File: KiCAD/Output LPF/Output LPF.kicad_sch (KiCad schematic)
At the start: 55 parts, among them J1 Conn_Coaxial_Small, J2 8P8C_Shielded, J28 Filter In, K1 G6K-2P-Y-T1, K2 G6K-2P-Y-T1, K3 G6K-2P-Y-T1, K4 G6K-2P-Y-T1, Q1 2N7000, Q10 2N7000, Q5 2N7000, Q8 2N7000

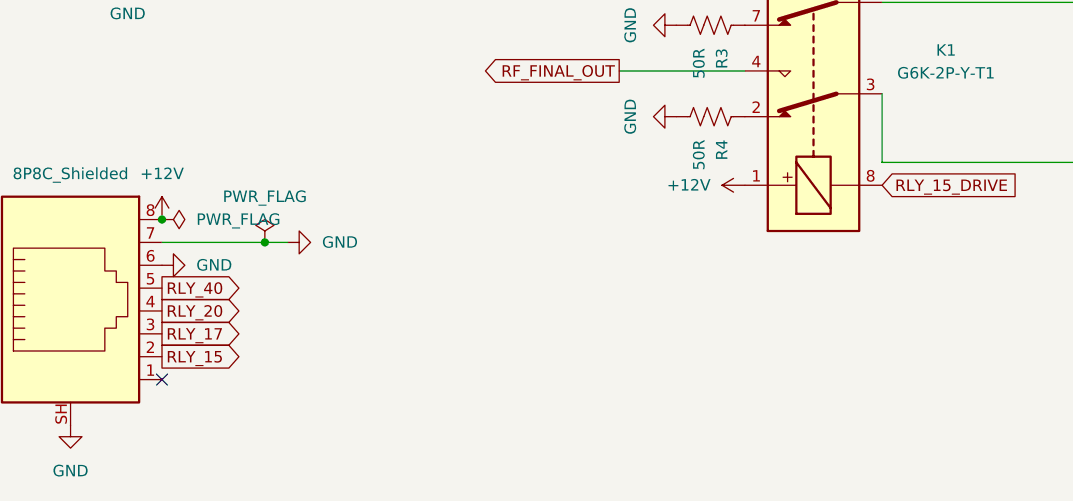
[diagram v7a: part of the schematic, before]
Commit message: revD: frontpanel + Output LPF text updates + protoshield in-progress
Output LPF: K relay Description text fix (pole 2 NC/COM/NO -> NO/COM/NC)
on K1/K2/K3 instances and the embedded lib symbol; CF7/CF8/CF12/CF16
Description "Unpolarized capacitor 2 in parallel to reach" stripped
back to "Unpolarized capacitor"; L6-L20 Descriptions updated T68-6 ->
T50-6 to match footprints.

xmitter.kicad_sym Relay_G6K Description text fix (pole 2 NC/COM/NO ->
NO/COM/NC) so future placements come out right.

Frontpanel: user updates (netlist regenerated).

Protoshield: in-progress schematic touches (new J7, #PWR017). Netlist
intentionally stale -- will regen after Metro-symbol SDA/SCL addition.

Co-Authored-By: Claude Opus 4.7 <noreply@anthropic.com>
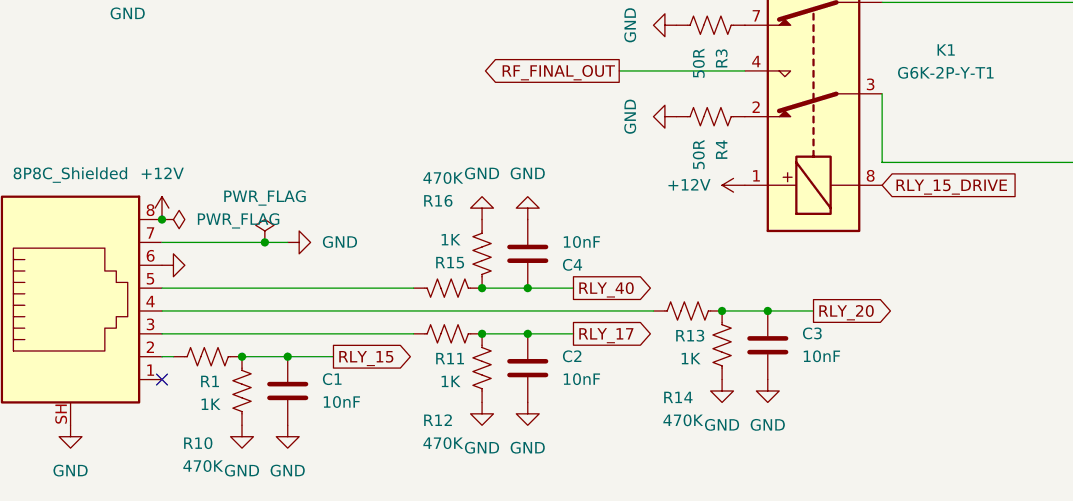
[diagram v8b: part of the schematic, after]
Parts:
- added C1, C2, C3, C4: 10nF, symbol Device:C
- added R1, R11, R13, R15: 1K, symbol Device:R_US
- added R10, R12, R14, R16: 470K, symbol Device:R_US
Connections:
- net GND: now also C1.2, C2.2, C3.2, C4.2, R10.2, R12.2, R14.2, R16.2
- net RLY_15: now also C1.1, R1.2, R10.1; no longer J2.2
- net RLY_17: now also C2.1, R11.2, R12.1; no longer J2.3
- net RLY_20: now also C3.1, R13.2, R14.1; no longer J2.4
- net RLY_40: now also C4.1, R15.2, R16.1; no longer J2.5
- new net: J2.5, R15.1
- new net: J2.4, R13.1
- new net: J2.2, R1.1
- new net: J2.3, R11.1
